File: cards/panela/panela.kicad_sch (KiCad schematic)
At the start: 123 parts, among them J1 BUS, Q1 2N7000, Q10 2N7000, Q11 2N7000, Q12 2N7000, Q13 2N7000, Q14 2N7000, Q15 2N7000, Q16 2N7000, Q17 2N7000, Q18 2N7000, Q19 2N7000, Q2 2N7000, Q20 2N7000, Q21 2N7000, Q22 2N7000, Q23 2N7000, Q24 2N7000, Q25 2N7000, Q26 2N7000, Q27 2N7000, Q28 2N7000, Q3 2N7000, Q4 2N7000, Q5 2N7000, Q6 2N7000, Q7 2N7000, Q8 2N7000, Q9 2N7000, SW1 A0 A1 A2 A3 B0 B1 B2 B3 (swit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, SW2 SUB EO AI AO BI BO BA AB

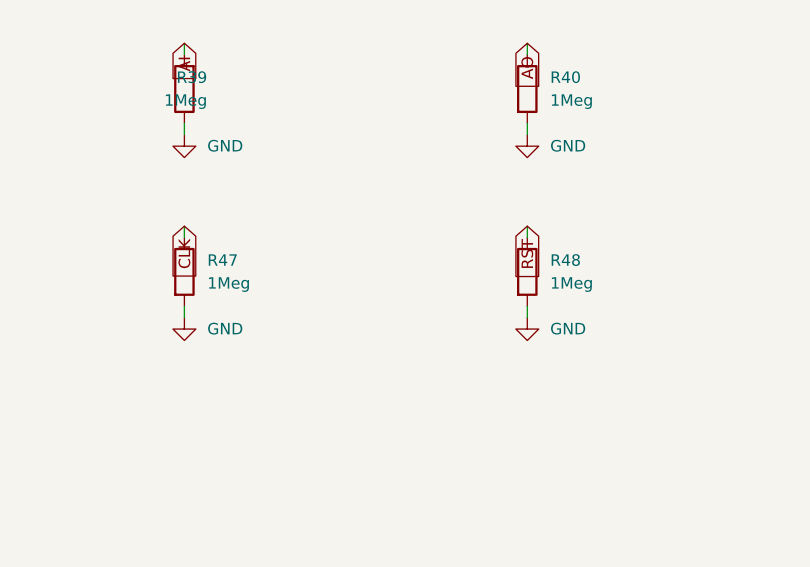
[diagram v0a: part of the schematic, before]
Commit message: Clock and panel: CLK and RST driven hard, the cards see one clock edge (D053)
The memory address latch race (D054, next commit) had a root under it:
the clock card's CLK pull-up was 10k into about 3 nF of card inputs and
ribbon, so the rising edge took 35 to 43 us from 0.5 to 3.5 V, and every
card reads that edge with its own transistors (Vto 0.8 to 3.0 V), so the
cards saw one edge up to 25 us apart. At mixed seed 2 the sequencer stepped
at 2 V and a register put the next tick's data on the bus 10 us later,
while the memory control card saw the edge at 3 V, 12 us after the bus had
changed. RST had the same trouble the other way: driven through 10k
against the panel's 1 Meg, it drifted for 8 ms after the reset Schmitt
let go (the machine once started a tick late, memory nibble-v2-plan
2026-09-14), so cards with different thresholds left reset on different
edges.

cards/clock (re-routed, DRC 0, 0 unconnected): the CLK pull-up is 1k, and
RST comes from a new inverter RD = NOT PB with a 1k pull-up through 100 ohm
and a diode. Lowering PA's own 47k instead took the gain out of the reset
Schmitt and RST followed the 220 ms capacitor ramp for milliseconds; the
buffer keeps the snap. cards/panela, panelb (values only, no layout
change): the CLK and RST pull-downs are 10k, the buttons' Schmitt output
inverters have 1k pull-ups and drive the lines through 100 ohm. About
20 mA more from the supply.

tb_clock now loads both lines with 3 nF and the panel's 10k, drives the
STEP button as the panel does, and measures CLK's rise (0.5 to 3.5 V,
must be under 10 us) and RST's release (3.5 to 0.8 V, under 100 us). On
the routed card's export: CLK rise 5.3 to 6.7 us, RST release 44 to 46 us,
period and duty unchanged (610 Hz TYP, 404 LO, 582 HI), one edge per STEP
press, at TYP, LO, HI, MIX 1 and 2, all PASS (sim/out/tb_clock_cards54_*.log).
The previous card on the same bench: CLK rise 43 us, RST never reached
0.8 V cleanly (sim/out/tb_clock_cards_oldD053_TYP.log).

machine.py: a dec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
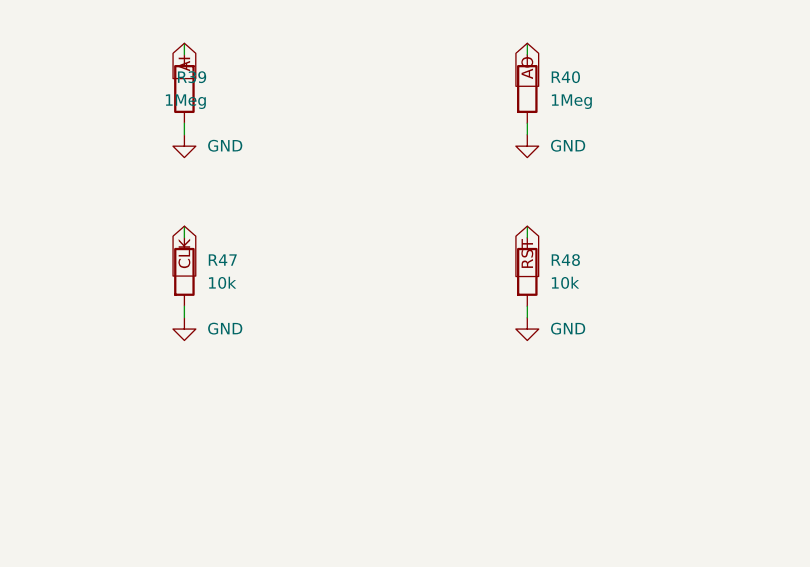
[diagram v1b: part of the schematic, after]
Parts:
- R47, R48: value 1Meg -> 10k
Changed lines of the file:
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@@
 			)
 		)
-		(property "Value" "1Meg"
+		(property "Value" "10k"
 			(at 127 359.41 0)
 			(show_name no)
@@
 			)
 		)
-		(property "Value" "1Meg"
+		(property "Value" "10k"
 			(at 165.1 359.41 0)
 			(show_name no)

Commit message: The bus headers go on the back of all 26 boards, no track moved; the silkscreen refitted (D059, D062)
An IDC socket lies across its ribbon, so the ribbon could never run along a
row of cards as drawn. It runs behind them, and the 64-pin headers are
soldered on the back. This commit is that move, made in place on the routed
boards: no board was routed again.

How the header sits (D062): in the holes it had, turned over top to bottom,
notch toward the top edge. A pin of the odd row is then in the hole its even
neighbour had, so the two signals of every pair of pins change places: CLK
is pin 6, RST pin 8, +5V pins 1, 2 and 64. bus.py keeps both tables: PINS,
what the header's pins carry, and HOLES, what the copper was routed to.

The proof, on all 26 boards against 992a90f (sim/board_diff.py):
  netlist the same, element for element; every track, every via and every
  hole the same; each copper and mask layer differs by two pad shapes per
  header (pin 1's square went to the hole beside it, both on +5V) and the
  ground pour's outline round those two pads, nowhere else by more than a
  tenth of a micrometre.
sim/rebuild_check.py runs every builder into a scratch directory: each
writes the plan and the netlist that are committed, so a rebuild gives
this board. order_check.py --machine holds every pad of the 27 headers to
bus.py and requires them on the back.

What the move costs: on the ribbon RST had a ground conductor on both
sides; now one neighbour is BUS1#. tb_rst_neighbour.py puts the two lines
on the bench with every gate the routed boards hang on them: RST rises
0.28 to 0.43 V when BUS1# is released, against a lowest threshold of 0.8 V
(sim/results/rst_neighbour.md). The machine deck's crosstalk option now
couples the pins that are neighbours on the ribbon; the crosstalk stage of
the machine gate has to be run again on that order.

Silkscreen (pcb.fit_silk): every label to 1.0 mm where it has room, off
pads, vias, outlines and other labels, out from under the pa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
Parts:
- SW1: value A0 A1 A2 A3 B0 B1 B2 B3 (switch up = 1) -> A0 A1 A2 A3 B0 B1 B2 B3 (switch ON = 1)
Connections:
- net +5V: now also J1.64 (Pin_64); no longer J1.63 (Pin_63)
- net A0: now also J1.14 (Pin_14); no longer J1.13 (Pin_13)
- net A1: now also J1.13 (Pin_13); no longer J1.14 (Pin_14)
- net A2: now also J1.16 (Pin_16); no longer J1.15 (Pin_15)
- net A3: now also J1.15 (Pin_15); no longer J1.16 (Pin_16)
- net AB: now also J1.45 (Pin_45); no longer J1.46 (Pin_46)
- net AI: now also J1.42 (Pin_42); no longer J1.41 (Pin_41)
- net AO: now also J1.41 (Pin_41); no longer J1.42 (Pin_42)
- net B0: now also J1.18 (Pin_18); no longer J1.17 (Pin_17)
- net B1: now also J1.17 (Pin_17); no longer J1.18 (Pin_18)
- net B2: now also J1.20 (Pin_20); no longer J1.19 (Pin_19)
- net B3: now also J1.19 (Pin_19); no longer J1.20 (Pin_20)
- net BA: now also J1.46 (Pin_46); no longer J1.45 (Pin_45)
- net BI: now also J1.44 (Pin_44); no longer J1.43 (Pin_43)
- net BO: now also J1.43 (Pin_43); no longer J1.44 (Pin_44)
- net BUS0#: now also J1.10 (Pin_10); no longer J1.9 (Pin_9)
- net BUS1#: now also J1.9 (Pin_9); no longer J1.10 (Pin_10)
- net BUS2#: now also J1.12 (Pin_12); no longer J1.11 (Pin_11)
- net BUS3#: now also J1.11 (Pin_11); no longer J1.12 (Pin_12)
- net CF: now also J1.38 (Pin_38); no longer J1.37 (Pin_37)
- net CLK: now also J1.6 (Pin_6); no longer J1.5 (Pin_5)
- net EO: now also J1.39 (Pin_39); no longer J1.40 (Pin_40)
- net GND: now also J1.5 (Pin_5), J1.63 (Pin_63), J1.7 (Pin_7); no longer J1.6 (Pin_6), J1.64 (Pin_64), J1.8 (Pin_8)
- net RST: now also J1.8 (Pin_8); no longer J1.7 (Pin_7)
- net SUB: now also J1.40 (Pin_40); no longer J1.39 (Pin_39)
- net ZF: now also J1.37 (Pin_37); no longer J1.38 (Pin_38)
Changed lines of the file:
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@@
 	(symbol
 		(lib_id "Connector_Generic:Conn_02x32_Odd_Even")
-		(at 76.2 101.6 0)
+		(at 78.74 101.6 0)
+		(mirror y)
 		(unit 1)
 		(body_style 1)
@@
 			)
 		)
-		(property "Value" "A0 A1 A2 A3 B0 B1 B2 B3 (switch up = 1)"
+		(property "Value" "A0 A1 A2 A3 B0 B1 B2 B3 (switch ON = 1)"
 			(at 27.94 417.83 0)
 			(show_name no)
